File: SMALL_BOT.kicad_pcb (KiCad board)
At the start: 2 copper layers, 80 x 65 mm, 37 parts, among them J1 MOTOR_B, J10 JMP, J11 UART, J12 LEDS, J13 I2C, J14 LEDS, J15 HEADER_1, J16 HEADER_1, J2 MOTOR_A, J3 HEADER_1, J4 HEADER_1, J5 HC-SR04, J6 HC-SR04, J7 HC-SR04, J8 HC-SR04, J9 Bateria, Q1 2N7002, U1 Teensy4.0_B, U2 DRV8872, U3 LM1117-SOT, U4 DRV8872

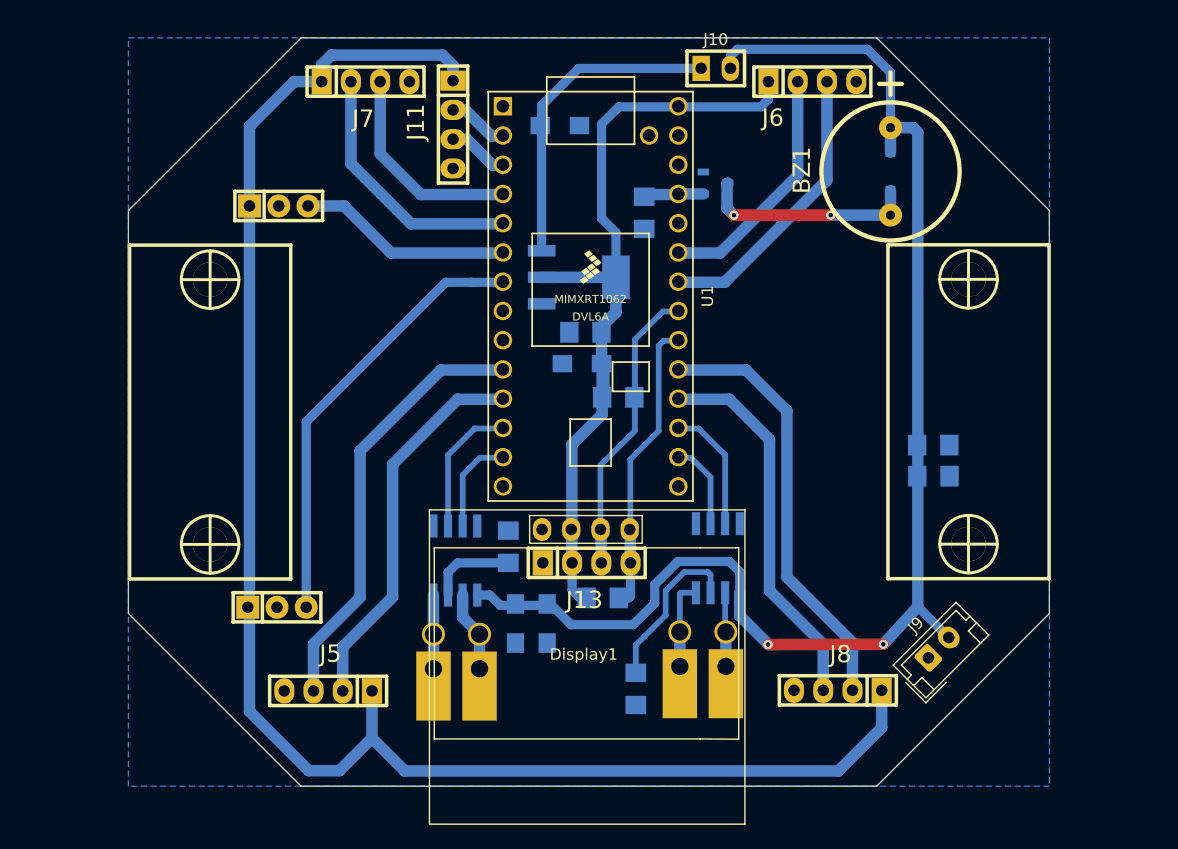
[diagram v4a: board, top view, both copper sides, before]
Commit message: modificaciones
se agrego una brebe pinout, se agrego una carpeta "doc" y lista de materiales, hay que agregarle los precios.tambien se modifico el pcb
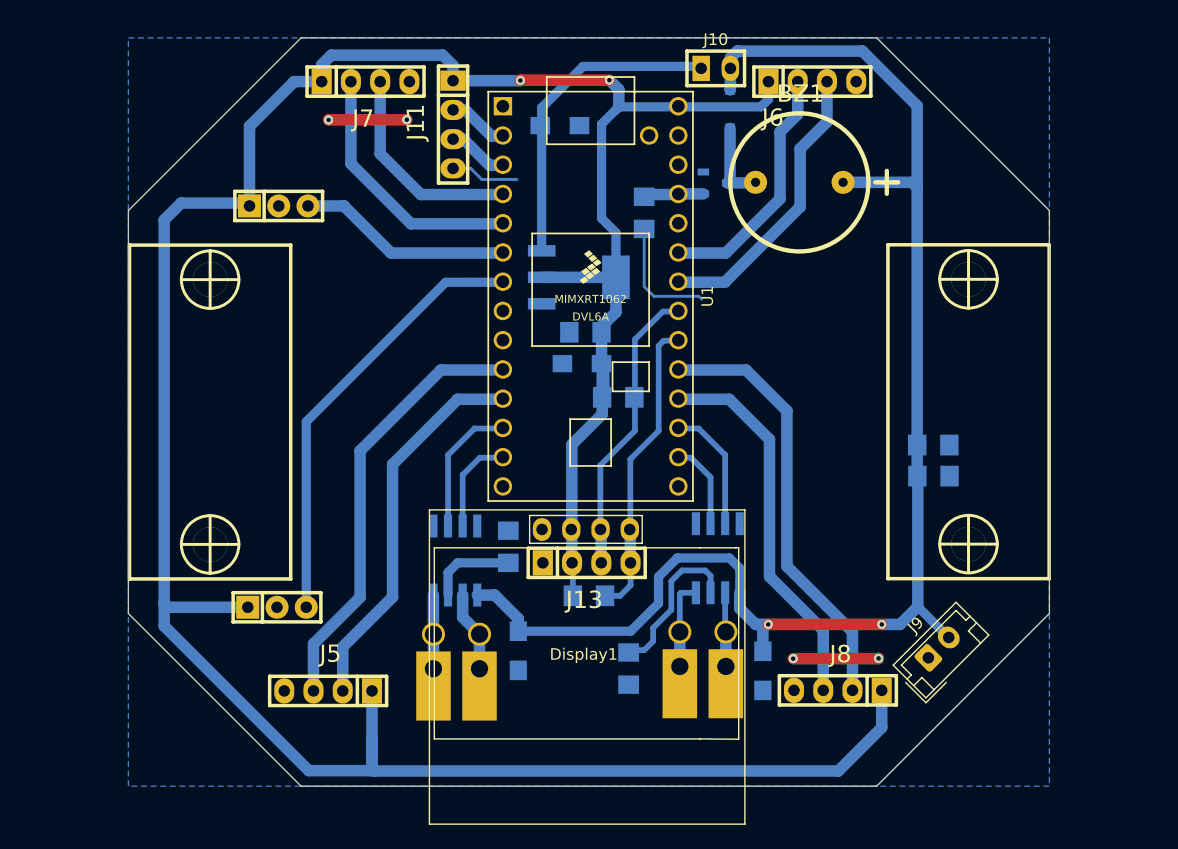
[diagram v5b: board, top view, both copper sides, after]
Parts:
- moved C7 19.2 mm to (135.1, 140.0)
- moved D1 15.0 mm to (132.3, 91.2)
- moved BZ1 7.98 mm to (138.3, 97.5), turned to 0 degrees
- moved C5 2.38 mm to (113.9, 138.2)
- moved R3 1.87 mm to (123.5, 139.8)
- moved R4 1.21 mm to (120.0, 133.5)
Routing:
- net +5V: track 211.7 -> 247.5 mm, vias 0 -> 2
- net GND: track 0.00 -> 30.6 mm, vias 0 -> 4
- net Net-(BZ1-Pad2): track 18.8 -> 7.26 mm, vias 2 -> 0
- net /VIN: track 122.7 -> 127.9 mm
- net /SDA: track 25.6 -> 26.2 mm
